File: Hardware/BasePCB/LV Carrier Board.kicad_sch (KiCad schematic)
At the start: 28 parts, among them J12 Conn_01x02, J2 Conn_01x04, J3 Conn_01x02, J4 CarCANConnector, J5 Conn_01x02, J8 Conn_01x02, J9 Conn_01x02

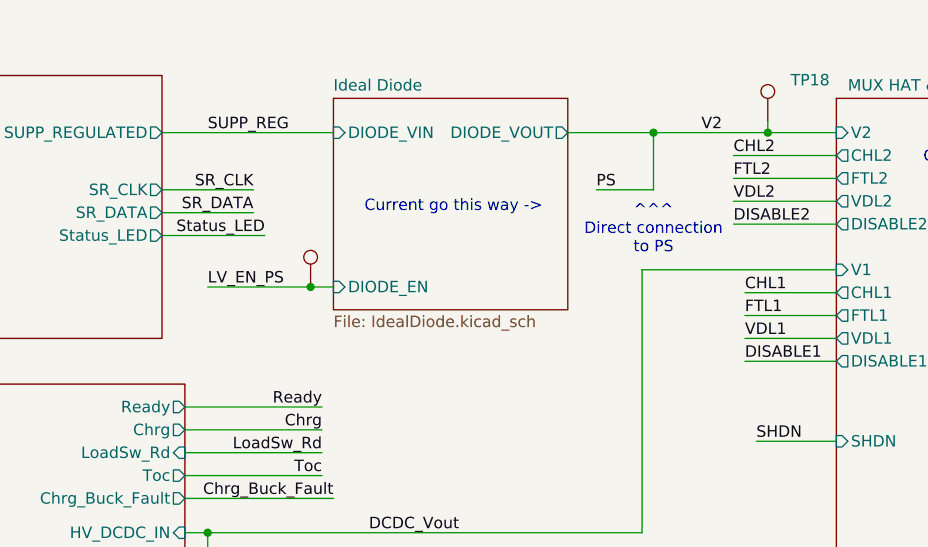
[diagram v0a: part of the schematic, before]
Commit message: change OV and fix silk
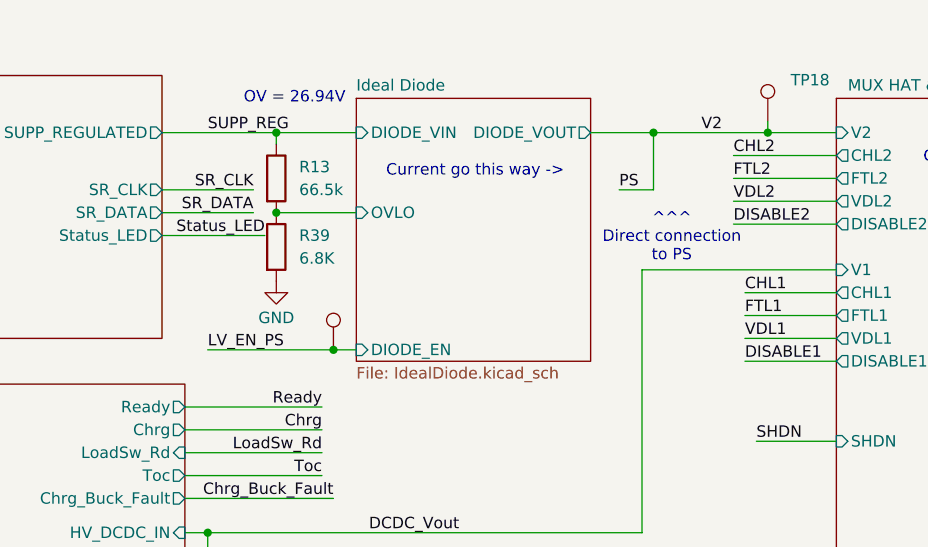
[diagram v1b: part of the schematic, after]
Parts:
- added R13: 66.5k, Resistor_SMD:R_0603_1608Metric_Pad0.98x0.95mm_HandSolder, symbol Device:R
- added R39: 6.8K, Resistor_SMD:R_0603_1608Metric_Pad0.98x0.95mm_HandSolder, symbol Device:R
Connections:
- net GND: now also R39.2
- net SUPP_REG: now also R13.1
- new net Ideal Diode/OVLO: R13.2, R39.1
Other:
- sheet Ideal Diode ports: added OVLO; removed none
- note added: "OV = 26.94V"

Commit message: BOM
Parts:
- LOGO1, LOGO2, TP10, TP18, TP24, TP26: now left out of the parts list
- R38: footprint Resistor_SMD:R_0805_2012Metric -> Resistor_SMD:R_0603_1608Metric_Pad0.98x0.95mm_HandSolder
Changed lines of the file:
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@@
 			)
 		)
-		(property "Footprint" "Resistor_SMD:R_0805_2012Metric"
+		(property "Footprint" "Resistor_SMD:R_0603_1608Metric_Pad0.98x0.95mm_HandSolder"
 			(at 48.26 60.198 90)
 			(effects
@@
 		(unit 1)
 		(exclude_from_sim no)
-		(in_bom yes)
+		(in_bom no)
 		(on_board yes)
 		(dnp no)
@@
 			)
 		)
-		(property "Datasheet" "~"
+		(property "Datasheet" "CRCW0603100KFKEE"
 			(at 41.91 109.22 0)
 			(effects
@@
 		(unit 1)
 		(exclude_from_sim no)
-		(in_bom yes)
+		(in_bom no)
 		(on_board yes)
 		(dnp no)
@@
 		(unit 1)
 		(exclude_from_sim no)
-		(in_bom yes)
+		(in_bom no)
 		(on_board yes)
 		(dnp no)
@@
 		(unit 1)
 		(exclude_from_sim no)
-		(in_bom yes)
+		(in_bom no)
 		(on_board yes)
 		(dnp no)
@@
 		(unit 1)
 		(exclude_from_sim no)
-		(in_bom yes)
+		(in_bom no)
 		(on_board yes)
 		(dnp no)
@@
 			)
 		)
-		(property "Datasheet" "~"
+		(property "Datasheet" "CRCW0603100KFKEE"
 			(at 50.8 109.22 0)
 			(effects
@@
 		(unit 1)
 		(exclude_from_sim no)
-		(in_bom yes)
-		(on_board yes)
-		(dnp no)
+		(in_bom no)
+		(on_board yes)
+		(dnp no)

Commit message: bom 2
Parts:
- C3: P/N (none) -> MAL217051152E3
- D1: P/N (none) -> BAT400D-7-F
- D13: P/N (none) -> B340BQ-13-F
- J12, J5, J8, J9: P/N (none) -> FIT0586
- J2: P/N (none) -> 105309-1104
- J3: P/N (none) -> PRT-10474
- R13: value 66.5k -> 198k; P/N CRCW060366K5FKEAC -> RT0603BRD07198KL
- R38: P/N (none) -> CRCW06030000Z0EE
- R39: value 6.8K -> 10k; P/N (none) -> CRCW060310K0FKEI
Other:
- moved on the sheet: C3
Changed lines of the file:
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@@
 	)
 	(junction
-		(at 262.89 33.02)
+		(at 261.62 33.02)
 		(diameter 0)
 		(color 0 0 0 0)
@@
 	(wire
 		(pts
+			(xy 261.62 33.02) (xy 272.415 33.02)
+		)
+		(stroke
+			(width 0)
+			(type default)
+		)
+	)
+	(wire
+		(pts
 			(xy 153.67 30.48) (xy 162.56 30.48)
 		)
@@
 	(wire
 		(pts
-			(xy 262.89 40.64) (xy 262.89 42.545)
+			(xy 261.62 40.64) (xy 261.62 43.18)
 		)
 		(stroke
@@
 	(wire
 		(pts
-			(xy 252.73 33.02) (xy 262.89 33.02)
+			(xy 252.73 33.02) (xy 261.62 33.02)
 		)
 		(stroke
@@
 	(wire
 		(pts
-			(xy 262.89 33.02) (xy 272.415 33.02)
-		)
-		(stroke
-			(width 0)
-			(type default)
-		)
-	)
-	(wire
-		(pts
 			(xy 140.97 41.91) (xy 152.4 41.91)
 		)
@@
 			)
 		)
+		(property "P/N" "FIT0586"
+			(at 277.495 35.56 0)
+			(effects
+				(font
+					(size 1.27 1.27)
+				)
+				(hide yes)
+			)
+		)
 		(pin "2"
 		)
@@
 			)
 		)
+		(property "P/N" "FIT0586"
+			(at 20.32 68.58 0)
+			(effects
+				(font
+					(size 1.27 1.27)
+				)
+				(hide yes)
+			)
+		)
 		(pin "1"
 		)
@@
 	(symbol
 		(lib_id "Device:R")
+		(at 153.67 43.18 0)
+		(unit 1)
+		(exclude_from_sim no)
+		(in_bom yes)
+		(on_board yes)
+		(dnp no)
+		(property "Reference" "R39"
+			(at 155.448 42.0116 0)
+			(effects
+				(font
+					(size 1.27 1.27)
+				)
+				(justify left)
+			)
+		)
+		(property "Value" "10k"
+			(at 155.448 44.323 0)
+			(effects
+				(font
+					(size 1.27 1.27)
+				)
+				(justify left)
+			)
+		)
+		(property "Footprint" "Resistor_SMD:R_0603_1608Metric_Pad0.98x0.95mm_HandSolder"
+			(at 151.892 43.18 90)
+			(effects
+				(font
+					(size 1.27 1.27)
+				)
+				(hide yes)
+			)
+		)
+		(property "Datasheet" "CRCW060310K0FKEI"
+			(at 153.67 43.18 0)
+			(effects
+				(font
+					(size 1.27 1.27)
+				)
+				(hide yes)
+			)
+		)
+		(property "Description" "Resistor"
+			(at 153.67 43.18 0)
+			(effects
+				(font
+					(size 1.27 1.27)
+				)
+				(hide yes)
+			)
+		)
+		(property "P/N" "CRCW060310K0FKEI "
+			(at 153.67 43.18 0)
+			(effects
+				(font
+					(size 1.27 1.27)
+				)
+				(hide yes)
+			)
+		)
+		(pin "1"
+		)
+		(pin "2"
+		)
+		(instances
+			(project "LV Carrier Board"
+				(path "/c5c5922b-1600-4b67-acf3-33264cecd75b"
+					(reference "R39")
+					(unit 1)
+				)
+			)
+		)
+	)
+	(symbol
+		(lib_id "Device:R")
 		(at 48.26 58.42 90)
 		(unit 1)
@@
 			)
 		)
-		(property "P/N" ""
+		(property "P/N" "CRCW06030000Z0EE"
 			(at 48.26 58.42 0)
 			(effects
@@
 	(symbol
 		(lib_id "Device:C")
-		(at 262.89 36.83 0)
+		(at 261.62 36.83 0)
 		(unit 1)
 		(exclude_from_sim no)
@@
 		(fields_autoplaced yes)
 		(property "Reference" "C3"
-			(at 266.7 35.5599 0)
+			(at 265.43 35.5599 0)
 			(effects
 				(font
@@
 		)
 		(property "Value" "1.5mF"
-			(at 266.7 38.0999 0)
+			(at 265.43 38.0999 0)
 			(effects
 				(font
@@
 		)
 		(property "Footprint" "Capacitor_THT:CP_Radial_D16.0mm_P7.50mm"
-			(at 263.8552 40.64 0)
+			(at 262.5852 40.64 0)
 			(effects
 				(font
@@
 		)
 		(property "Datasheet" "~"
-			(at 262.89 36.83 0)
+			(at 261.62 36.83 0)
 			(effects
 				(font
@@
 		)
 		(property "Description" "Unpolarized capacitor"
-			(at 262.89 36.83 0)
+			(at 261.62 36.83 0)
+			(effects
+				(font
+					(size 1.27 1.27)
+				)
+				(hide yes)
+			)
+		)
+		(property "P/N" "MAL217051152E3"
+			(at 261.62 36.83 0)
 			(effects
 				(font
@@
 			)
 		)
+		(property "P/N" "B340BQ-13-F "
+			(at 48.26 53.34 0)
+			(effects
+				(font
+					(size 1.27 1.27)
+				)
+				(hide yes)
+			)
+		)
 		(pin "2"
 		)
@@
 	(symbol
 		(lib_id "power:GND")
-		(at 262.89 42.545 0)
+		(at 261.62 43.18 0)
 		(unit 1)
 		(exclude_from_sim no)
@@
 		(fields_autoplaced yes)
 		(property "Reference" "#PWR043"
-			(at 262.89 48.895 0)
+			(at 261.62 49.53 0)
 			(effects
 				(font
@@
 		)
 		(property "Value" "GND"
-			(at 262.89 47.625 0)
+			(at 261.62 48.26 0)
 			(effects
 				(font
@@
 		)
 		(property "Footprint" ""
-			(at 262.89 42.545 0)
+			(at 261.62 43.18 0)
 			(effects
 				(font
@@
 		)
 		(property "Datasheet" ""
-			(at 262.89 42.545 0)
+			(at 261.62 43.18 0)
 			(effects
 				(font
@@
 		)
 		(property "Description" "Power symbol creates a global label with name \"GND\" , ground"
-			(at 262.89 42.545 0)
+			(at 261.62 43.18 0)
 			(effects
 				(font
@@
 			)
 		)
-		(property "Datasheet" "~"
+		(property "Datasheet" "https://www.digikey.com/en/products/detail/diodes-incorporated/BAT400D-7-F/725016"
 			(at 132.08 114.3 0)
 			(effects
@@
 			)
 		)
+		(property "P/N" "BAT400D-7-F "
+			(at 133.35 114.3 0)
+			(effects
+				(font
+					(size 1.27 1.27)
+				)
+				(hide yes)
+			)
+		)
 		(pin "3"
 		)
@@
 			)
 		)
+		(property "P/N" "FIT0586"
+			(at 20.32 55.88 0)
+			(effects
+				(font
+					(size 1.27 1.27)
+				)
+				(hide yes)
+			)
+		)
 		(pin "1"
 		)
@@
 			)
 		)
-		(property "Value" "66.5k"
+		(property "Value" "198k"
 			(at 156.21 36.8299 0)
 			(effects
@@
 			)
 		)
-		(property "Datasheet" "https://www.mouser.com/ProductDetail/Vishay/CRCW060366K5FKEAC?qs=E3Y5ESvWgWOGbq5Mg2tjWg%3D%3D"
+		(property "Datasheet" "https://www.mouser.com/ProductDetail/YAGEO/RT0603BRD07198KL?qs=bQfrgN9vNvxjjoB%252BIKRwPQ%3D%3D"
 			(at 153.67 35.56 0)
 			(effects
@@
 			)
 		)
-		(property "P/N" "CRCW060366K5FKEAC"
+		(property "P/N" "RT0603BRD07198KL"
 			(at 153.67 35.56 0)
 			(effects
@@
 			)
 		)
+		(property "P/N" "PRT-10474 "
+			(at 21.59 91.44 0)
+			(effects
+				(font
+					(size 1.27 1.27)
+				)
+				(hide yes)
+			)
+		)
 		(pin "2"
 		)
@@
 			)
 		)
+		(property "P/N" "FIT0586"
+			(at 20.32 30.48 0)
+			(effects
+				(font
+					(size 1.27 1.27)
+				)
+				(hide yes)
+			)
+		)
 		(pin "1"
 		)
@@
 	(symbol
 		(lib_id "Device:R")
-		(at 153.67 43.18 0)
-		(unit 1)
-		(exclude_from_sim no)
-		(in_bom yes)
-		(on_board yes)
-		(dnp no)
-		(fields_autoplaced yes)
-		(property "Reference" "R39"
-			(at 156.21 41.9099 0)
-			(effects
-				(font
-					(size 1.27 1.27)
-				)
-				(justify left)
-			)
-		)
-		(property "Value" "6.8K"
-			(at 156.21 44.4499 0)
-			(effects
-				(font
-					(size 1.27 1.27)
-				)
-				(justify left)
-			)
-		)
-		(property "Footprint" "Resistor_SMD:R_0603_1608Metric_Pad0.98x0.95mm_HandSolder"
-			(at 151.892 43.18 90)
-			(effects
-				(font
-					(size 1.27 1.27)
-				)
-				(hide yes)
-			)
-		)
-		(property "Datasheet" "~"
-			(at 153.67 43.18 0)
-			(effects
-				(font
-					(size 1.27 1.27)
-				)
-				(hide yes)
-			)
-		)
-		(property "Description" "Resistor"
-			(at 153.67 43.18 0)
-			(effects
-				(font
-					(size 1.27 1.27)
-				)
-				(hide yes)
-			)
-		)
-		(pin "2"
-		)
-		(pin "1"
-		)
-		(instances
-			(project "LV Carrier Board"
-				(path "/c5c5922b-1600-4b67-acf3-33264cecd75b"
-					(reference "R39")
-					(unit 1)
-				)
-			)
-		)
-	)
-	(symbol
-		(lib_id "Device:R")
 		(at 50.8 109.22 0)
 		(unit 1)
@@
 			(at 22.86 118.11 0)
 			(effects
+				(font
+					(size 1.27 1.27)
+				)
+				(hide yes)
+			)
+		)
+		(property "P/N" "105309-1104 "
+			(at 22.86 118.11 0)
+			(effects

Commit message: fix basePCB libs
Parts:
- D13: footprint PowerBoardLib:P26_DO-214AA_SMB -> LV Carrier Library:B340BQ-13-F
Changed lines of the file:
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@@
 			)
 		)
-		(property "Footprint" "PowerBoardLib:P26_DO-214AA_SMB"
+		(property "Footprint" "LV Carrier Library:B340BQ-13-F"
 			(at 48.26 53.34 0)
 			(effects

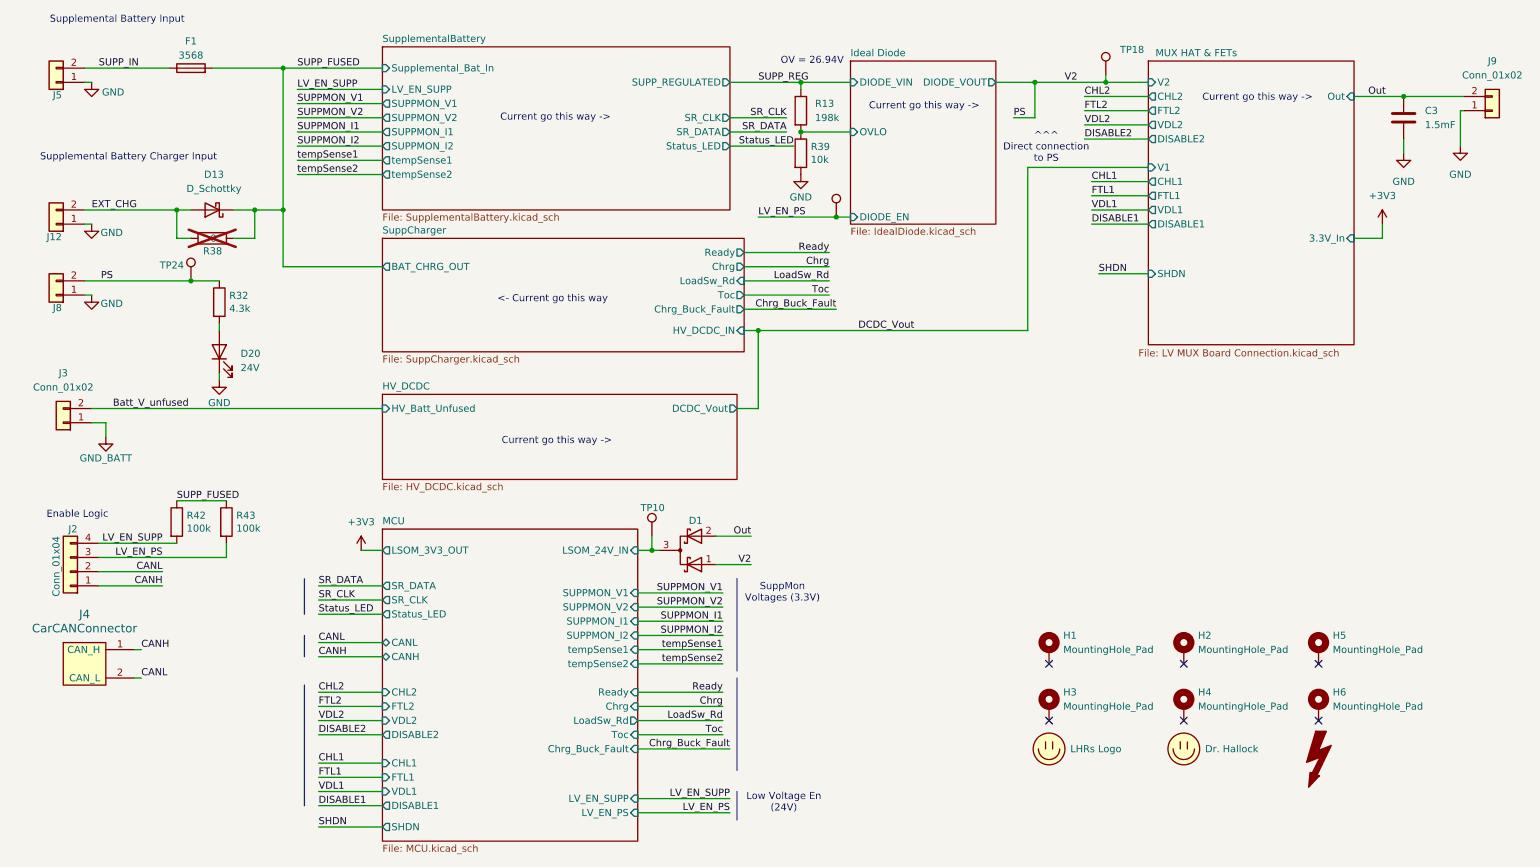
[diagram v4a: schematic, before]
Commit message: add hall effect sensor
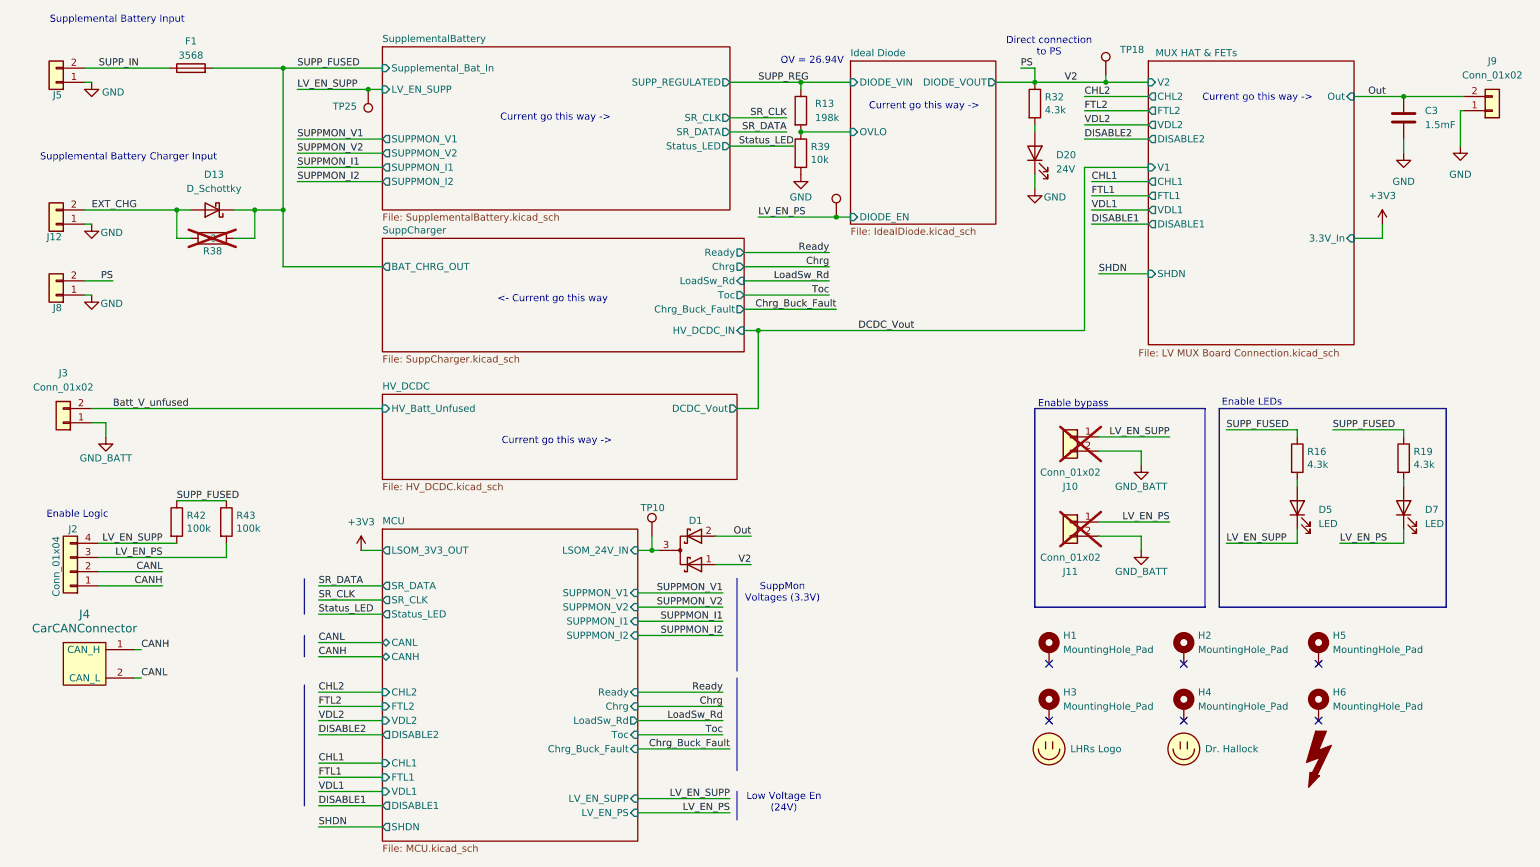
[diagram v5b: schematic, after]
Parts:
- removed TP24: TestPoint, TestPoint:TestPoint_THTPad_D3.0mm_Drill1.5mm, symbol Connector:TestPoint
- added D5, D7: LED, LED_SMD:LED_0603_1608Metric_Pad1.05x0.95mm_HandSolder, symbol Device:LED
- added J10, J11: Conn_01x02, Connector_PinHeader_2.54mm:PinHeader_1x02_P2.54mm_Vertical, symbol Connector_Generic:Conn_01x02
- added R16, R19: 4.3k, Resistor_SMD:R_0603_1608Metric_Pad0.98x0.95mm_HandSolder, symbol Device:R
- added TP25: TestPoint, TestPoint:TestPoint_THTPad_D3.0mm_Drill1.5mm, symbol Connector:TestPoint
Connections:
- net GND_BATT: now also J10.2 (Pin_2), J11.2 (Pin_2)
- net LV_EN_PS: now also D7.1 (K), J11.1 (Pin_1)
- net LV_EN_SUPP: now also D5.1 (K), J10.1 (Pin_1), TP25.1
- net SUPP_FUSED: now also R16.1, R19.1
- new net: D5.2 (A), R16.2
- new net: D7.2 (A), R19.2
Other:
- sheet MCU ports: added none; removed tempSense1, tempSense2
- sheet SupplementalBattery ports: added none; removed tempSense1, tempSense2
- note added: "Direct connection to PS"
- note added: "Enable LEDs"
- note added: "Enable bypass"
- note removed: "^^^ Direct connection to PS"
- moved on the sheet: D20, R32
